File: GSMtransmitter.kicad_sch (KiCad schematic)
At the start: 44 parts, among them J1 Conn_01x06_Pin, J2 Conn_02x02_2.54, J3 Conn_01x05, SW1 SM5-180UP-1, U1 STM32L051C8Tx, Y1 8 MHz, Y2 32768 kHz

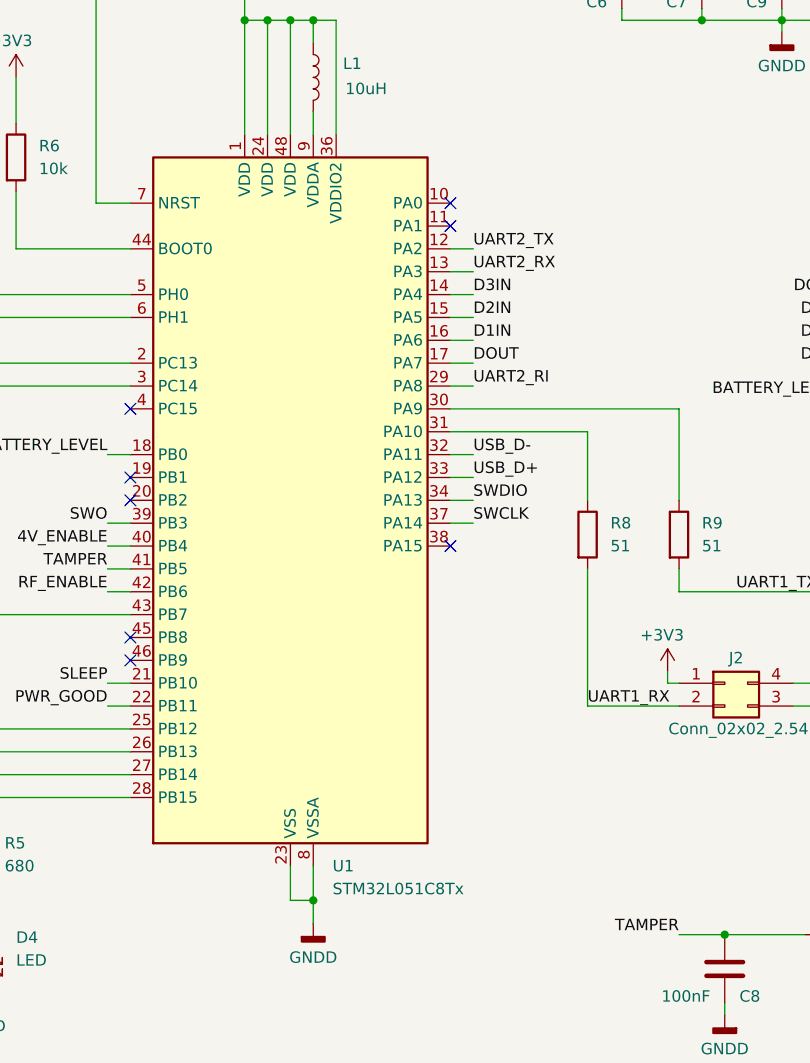
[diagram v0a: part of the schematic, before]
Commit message: STM32L052 instead STM32L051
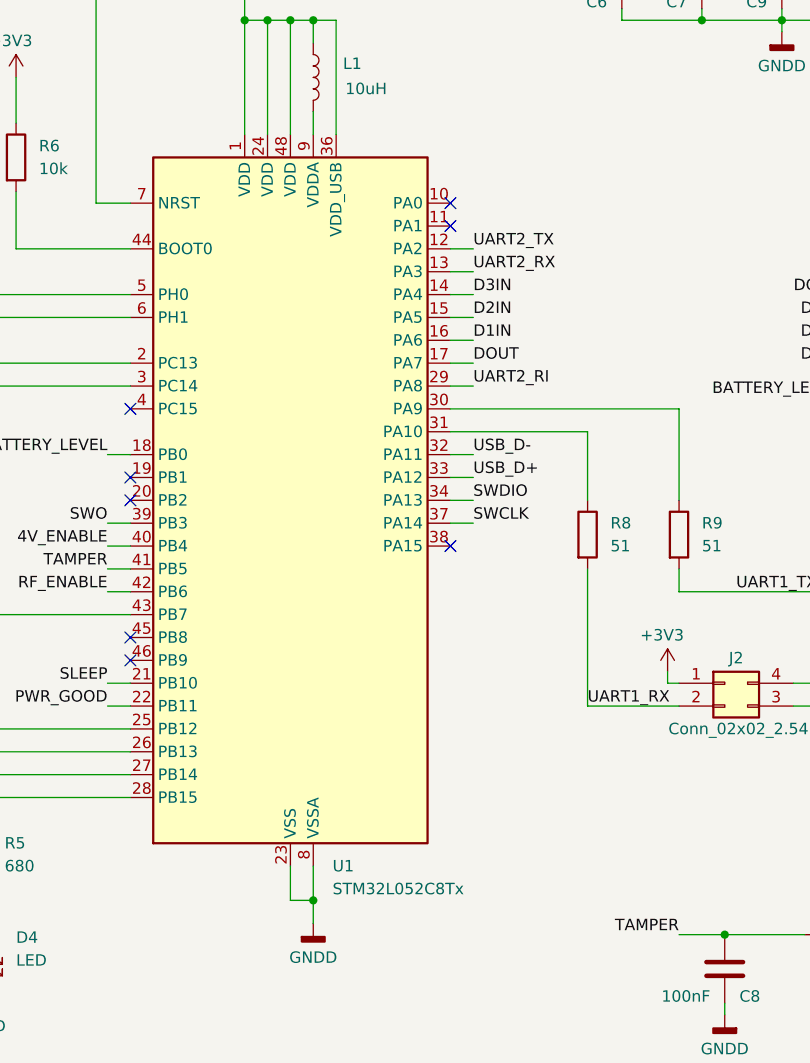
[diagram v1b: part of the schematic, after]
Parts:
- removed U1: STM32L051C8Tx, Package_QFP:LQFP-48_7x7mm_P0.5mm, symbol MCU_ST_STM32L0:STM32L051C8Tx
- added U1: STM32L052C8Tx, Package_QFP:LQFP-48_7x7mm_P0.5mm, symbol MCU_ST_STM32L0:STM32L052C8Tx
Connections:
- net +3V3: now also U1.1 (VDD), U1.24 (VDD), U1.36 (VDD_USB), U1.48 (VDD)
- net 4V_ENABLE: now also U1.40 (PB4)
- net BATTERY_LEVEL: now also U1.18 (PB0)
- net D1IN: now also U1.16 (PA6)
- net D2IN: now also U1.15 (PA5)
- net D3IN: now also U1.14 (PA4)
- net DOUT: now also U1.17 (PA7)
- net GNDD: now also U1.23 (VSS), U1.35 (VSS), U1.47 (VSS), U1.8 (VSSA)
- net NRST: now also U1.7 (NRST)
- net PWR_GOOD: now also U1.22 (PB11)
- net RF_ENABLE: now also U1.42 (PB6)
- net SLEEP: now also U1.21 (PB10)
- net SWCLK: now also U1.37 (PA14)
- net SWDIO: now also U1.34 (PA13)
- net SWO: now also U1.39 (PB3)
- net TAMPER: now also U1.41 (PB5)
- net UART2_RI: now also U1.29 (PA8)
- net UART2_RX: now also U1.13 (PA3)
- net UART2_TX: now also U1.12 (PA2)
- net USB_D+: now also U1.33 (PA12)
- net USB_D-: now also U1.32 (PA11)
- net at R5.1: now also U1.28 (PB15)
- net at C2.2, Y1.1: now also U1.6 (PH1)
- net at C1.2, Y1.2: now also U1.5 (PH0)
- net at C3.2, Y2.2: now also U1.2 (PC13)
- net at R2.1: now also U1.25 (PB12)
- net at R3.1: now also U1.26 (PB13)
- net at R4.1: now also U1.27 (PB14)
- net at C4.2, Y2.1: now also U1.3 (PC14)
- net at R9.1: now also U1.30 (PA9)
- net at R8.1: now also U1.31 (PA10)
- net at JP1.2 (B), R1.2: now also U1.43 (PB7)
- net at R6.2: now also U1.44 (BOOT0)
- net at L1.2: now also U1.9 (VDDA)

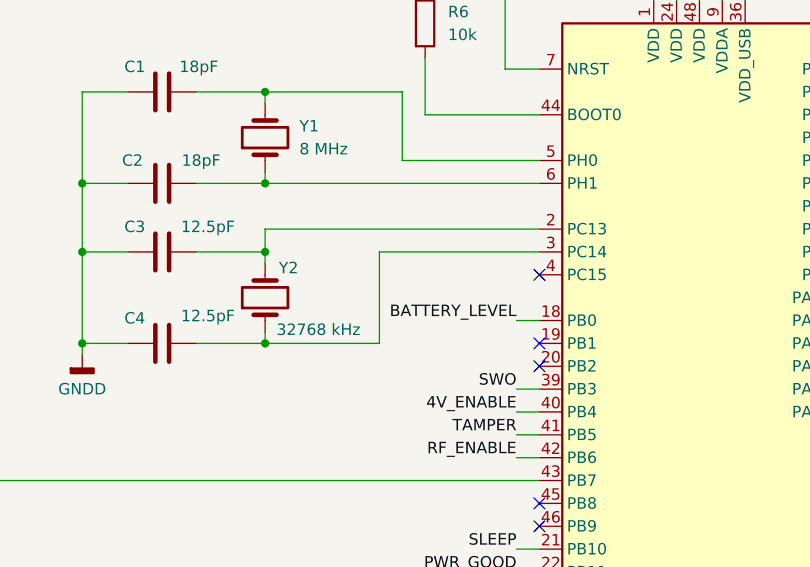
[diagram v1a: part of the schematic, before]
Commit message: Wrong 32kHz clock pins fixed
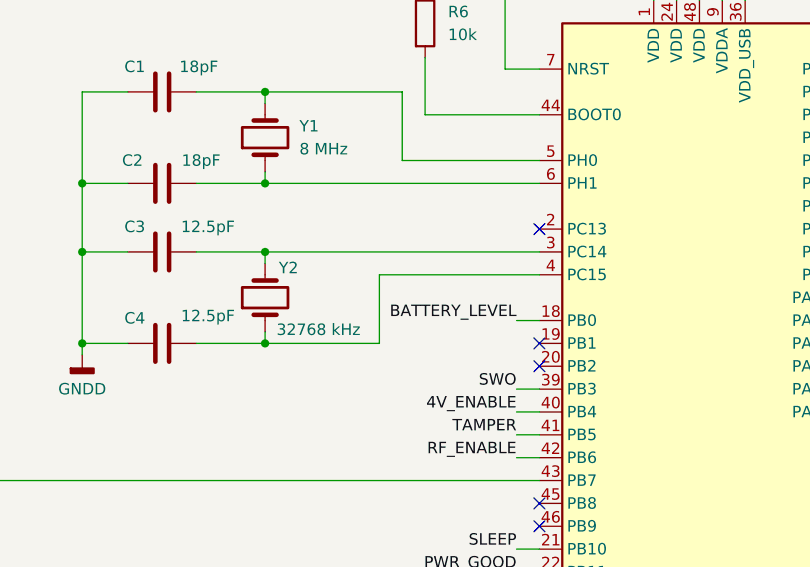
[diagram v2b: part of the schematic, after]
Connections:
- net at C4.2, Y2.1: now also U1.4 (PC15); no longer U1.3 (PC14)
- net at C3.2, Y2.2: now also U1.3 (PC14); no longer U1.2 (PC13)
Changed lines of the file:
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@@
+	)
+	(no_connect
+		(at 109.22 81.28)
 	)
 	(no_connect
 		(at 109.22 96.52)
 	)
-	(no_connect
-		(at 109.22 86.36)
-	)
 	(wire
 		(pts
@@
 	(wire
 		(pts
-			(xy 91.44 93.98) (xy 91.44 83.82)
+			(xy 91.44 93.98) (xy 91.44 86.36)
 		)
 		(stroke
@@
 	(wire
 		(pts
-			(xy 78.74 81.28) (xy 109.22 81.28)
-		)
-		(stroke
-			(width 0)
-			(type default)
-		)
-	)
-	(wire
-		(pts
 			(xy 170.18 144.78) (xy 175.26 144.78)
 		)
@@
 	(wire
 		(pts
+			(xy 91.44 86.36) (xy 109.22 86.36)
+		)
+		(stroke
+			(width 0)
+			(type default)
+		)
+	)
+	(wire
+		(pts
 			(xy 144.78 83.82) (xy 147.32 83.82)
 		)
@@
 	(wire
 		(pts
-			(xy 78.74 83.82) (xy 78.74 81.28)
-		)
-		(stroke
-			(width 0)
-			(type default)
-		)
-	)
-	(wire
-		(pts
 			(xy 36.83 50.8) (xy 39.37 50.8)
 		)
@@
 	(wire
 		(pts
+			(xy 78.74 83.82) (xy 109.22 83.82)
+		)
+		(stroke
+			(width 0)
+			(type default)
+		)
+	)
+	(wire
+		(pts
 			(xy 163.83 43.18) (xy 172.72 43.18)
 		)
@@
 		)
 		(stroke
-			(width 0)
-			(type default)
-		)
-	)
-	(wire
-		(pts
-			(xy 91.44 83.82) (xy 109.22 83.82)
-		)
-		(stroke

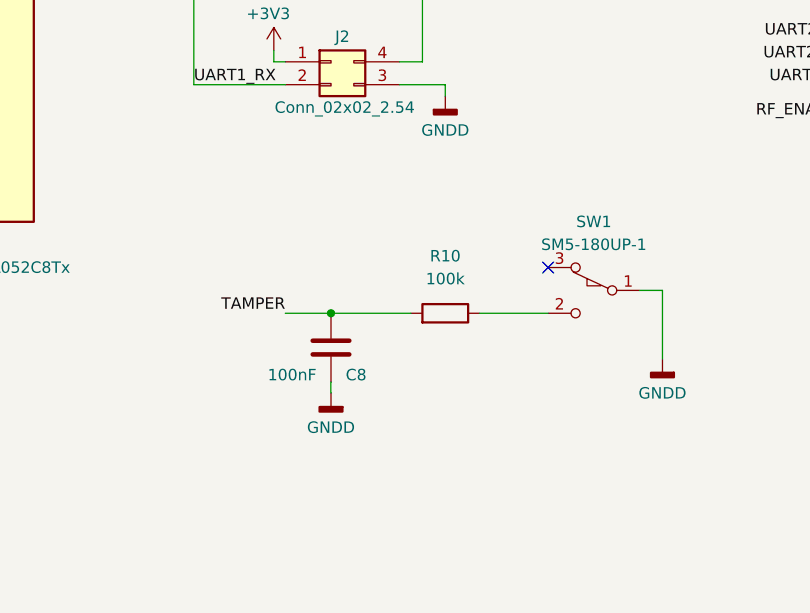
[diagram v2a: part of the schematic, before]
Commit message: 32kHz replaced
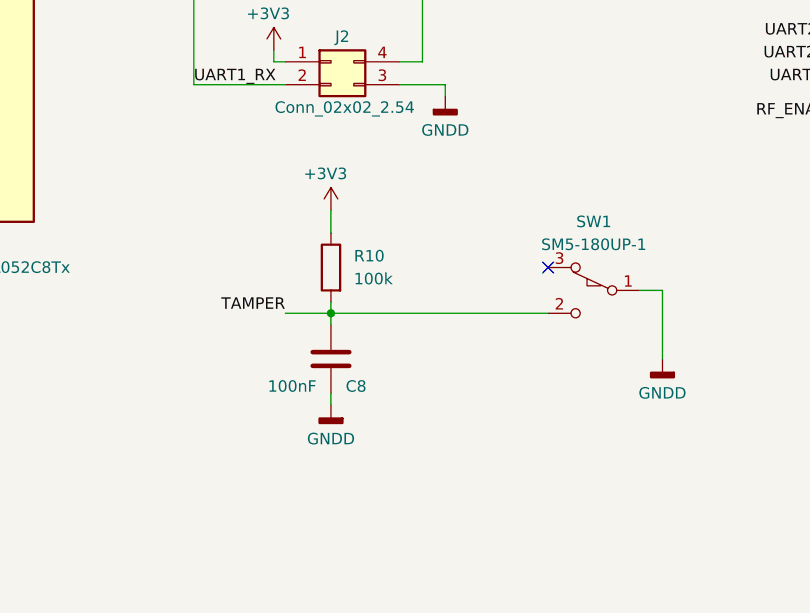
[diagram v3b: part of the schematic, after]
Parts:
- Y2: footprint Crystal:Crystal_Round_D2.0mm_Vertical -> Crystal:Crystal_SMD_EuroQuartz_EQ161-2Pin_3.2x1.5mm_HandSoldering
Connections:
- net +3V3: now also R10.1
- net TAMPER: now also SW1.2 (B)
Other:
- moved on the sheet: C8, R10

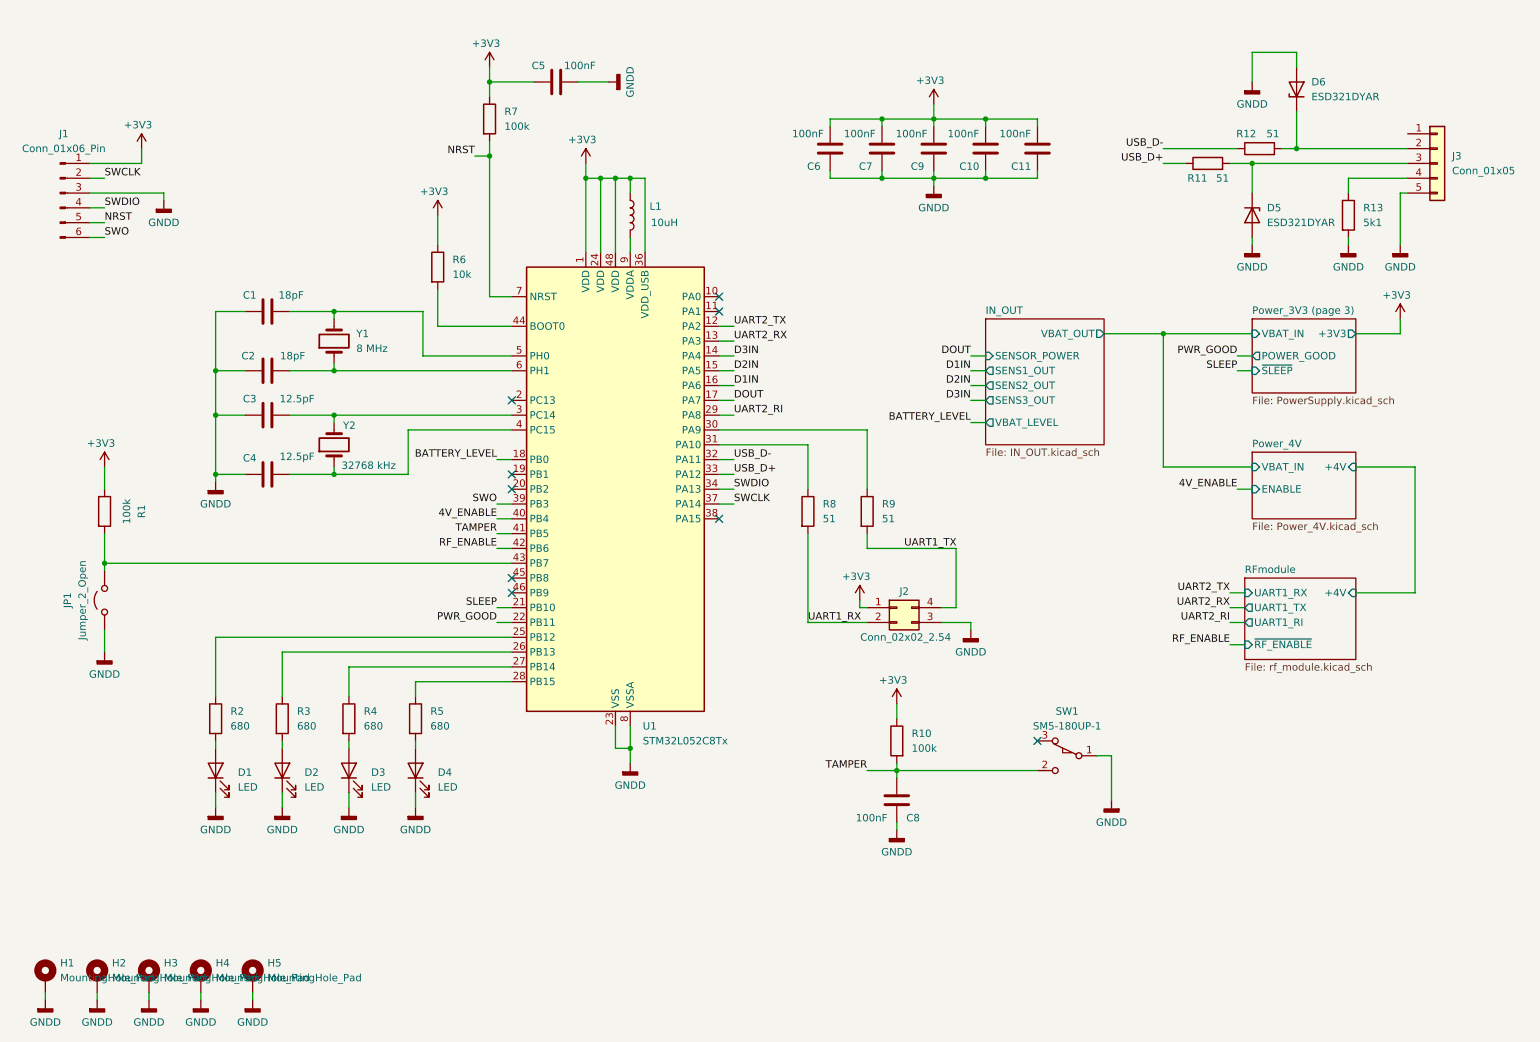
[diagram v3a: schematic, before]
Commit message: Inductance was replaced
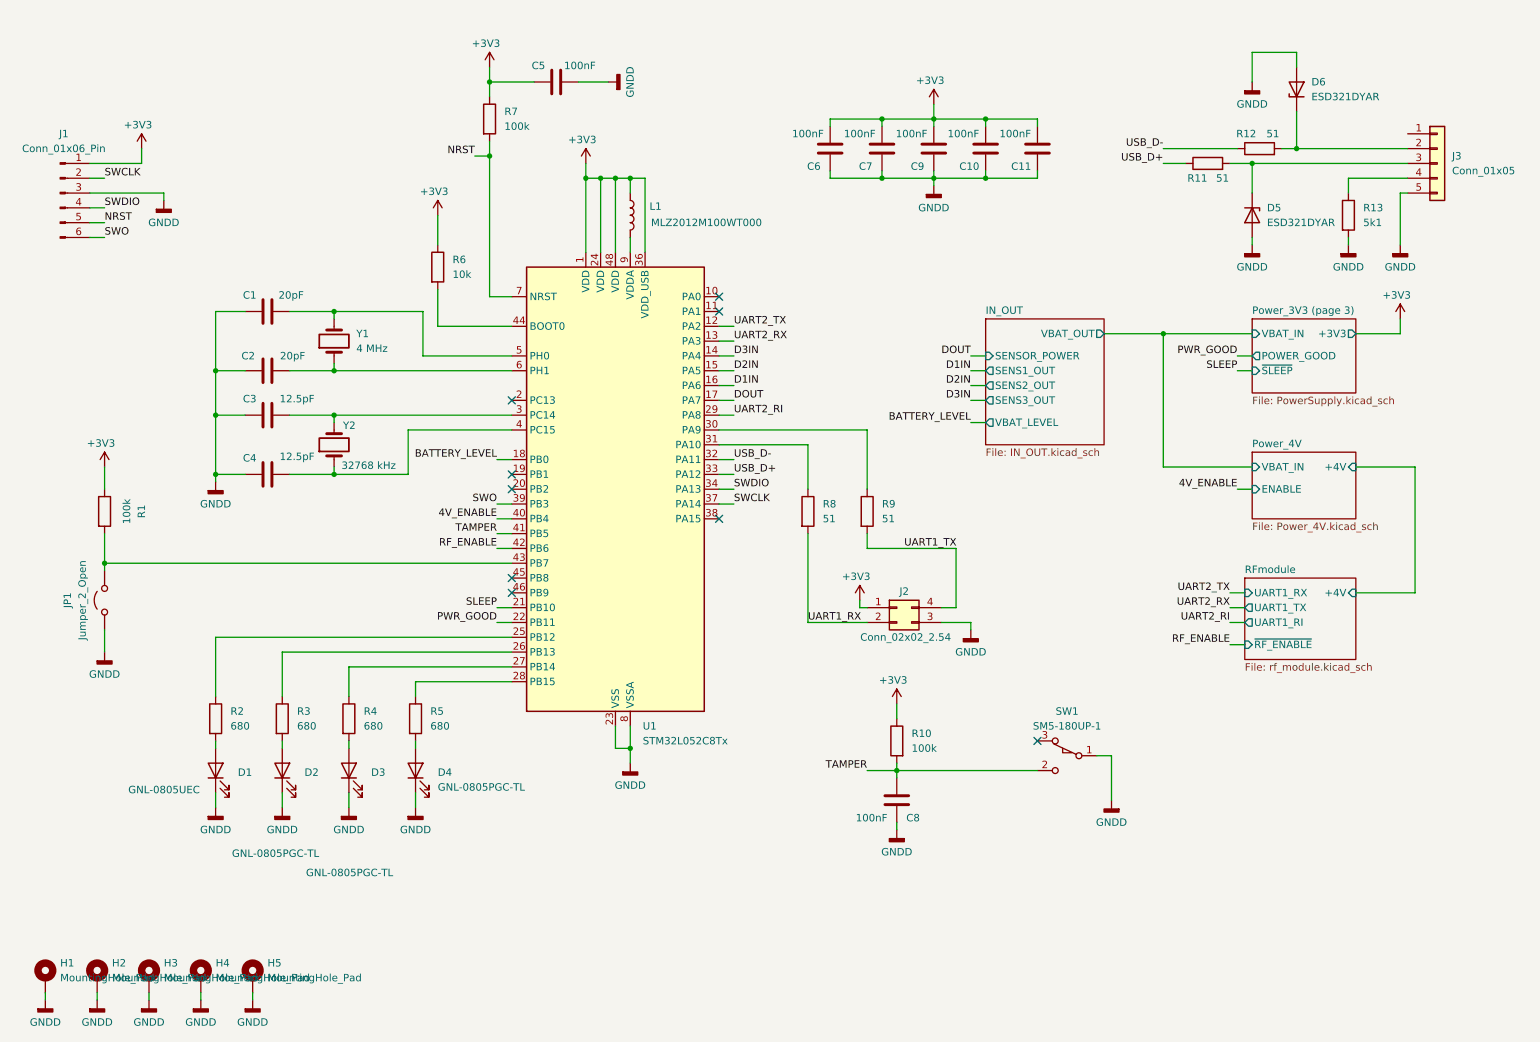
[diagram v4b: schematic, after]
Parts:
- C1, C2: value 18pF -> 20pF
- D1: value LED -> GNL-0805UEC
- D2, D3, D4: value LED -> GNL-0805PGC-TL
- L1: value 10uH -> MLZ2012M100WT000
- Y1: value 8 MHz -> 4 MHz
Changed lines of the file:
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@@
 			)
 		)
-		(property "Value" "8 MHz"
+		(property "Value" "4 MHz"
 			(at 82.55 72.3899 90)
 			(effects
@@
 			)
 		)
-		(property "Value" "LED"
+		(property "Value" "GNL-0805PGC-TL"
 			(at 96.52 147.6374 90)
 			(effects
@@
 			)
 		)
-		(property "Value" "18pF"
+		(property "Value" "20pF"
 			(at 71.374 63.246 90)
 			(effects
@@
 		(on_board yes)
 		(dnp no)
-		(fields_autoplaced yes)
 		(property "Reference" "D1"
 			(at 62.23 145.0974 90)
@@
 			)
 		)
-		(property "Value" "LED"
-			(at 62.23 147.6374 90)
+		(property "Value" "GNL-0805UEC"
+			(at 43.434 148.082 90)
 			(effects
 				(font
@@
 		(on_board yes)
 		(dnp no)
-		(fields_autoplaced yes)
 		(property "Reference" "D3"
 			(at 85.09 145.0974 90)
@@
 			)
 		)
-		(property "Value" "LED"
-			(at 85.09 147.6374 90)
+		(property "Value" "GNL-0805PGC-TL"
+			(at 73.914 162.306 90)
 			(effects
 				(font
@@
 			)
 		)
-		(property "Value" "10uH"
+		(property "Value" "MLZ2012M100WT000"
 			(at 133.096 50.8 0)
 			(effects
@@
 			)
 		)
-		(property "Value" "18pF"
+		(property "Value" "20pF"
 			(at 71.628 73.66 90)
 			(effects
@@
 		(on_board yes)
 		(dnp no)
-		(fields_autoplaced yes)
 		(property "Reference" "D2"
 			(at 73.66 145.0974 90)
@@
 			)
 		)
-		(property "Value" "LED"
-			(at 73.66 147.6374 90)
+		(property "Value" "GNL-0805PGC-TL"
+			(at 61.214 159.004 90)
 			(effects
 				(font
